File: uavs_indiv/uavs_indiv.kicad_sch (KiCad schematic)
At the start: 16 parts, among them J4 Conn_01x04_Pin, J5 Conn_01x04_Pin, J6 Conn_01x04_Pin, U1 LM2576HVS-5, U3 LM2576HVS-5

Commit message: wtf did i just see
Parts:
- removed J4, J5: Conn_01x04_Pin, customdcdc:Molex_Micro-Fit_3.0_43650-0400_1x04_P3.00mm_Horizontal, symbol Connector:Conn_01x04_Pin
- added J1: Conn_01x02_Socket, Connector_AMASS:AMASS_XT60PW-F_1x02_P7.20mm_Horizontal, symbol Connector:Conn_01x02_Socket
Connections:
- net +5V: now also J6.1 (Pin_1), J6.2 (Pin_2)
- net GND: now also J1.1 (Pin_1)
- net Vin: now also J1.2 (Pin_2); no longer J6.1 (Pin_1), J6.2 (Pin_2)
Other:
- moved on the sheet: C5, C6, J6

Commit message: redidt footprints and routing
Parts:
- added J2, J3: Conn_01x04_Pin, customdcdc:Molex_Micro-Fit_3.0_43650-0400_1x04_P3.00mm_Horizontal, symbol Connector:Conn_01x04_Pin
- C1, C8: value 330uF -> 1000uF; footprint Capacitor_THT:CP_Axial_L29.0mm_D10.0mm_P35.00mm_Horizontal -> customdcdc:capacitor1000uf
- C2, C7: footprint Capacitor_THT:CP_Axial_L29.0mm_D10.0mm_P35.00mm_Horizontal -> customdcdc:capacitor100uf
- C5: footprint Capacitor_THT:CP_Axial_L29.0mm_D10.0mm_P35.00mm_Horizontal -> customdcdc:capacitor220uf
- C6: footprint Capacitor_THT:CP_Axial_L20.0mm_D10.0mm_P26.00mm_Horizontal -> customdcdc:capacitor680uf
- L1, L3: value 330u -> 100u; footprint Inductor_THT:L_Axial_L20.0mm_D8.0mm_P5.08mm_Vertical -> customdcdc:inductor3.5a100u
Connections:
- net +5V: now also J2.1 (Pin_1), J2.2 (Pin_2), J3.1 (Pin_1), J3.2 (Pin_2)
- net GND: now also J2.3 (Pin_3), J2.4 (Pin_4), J3.3 (Pin_3), J3.4 (Pin_4)
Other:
- moved on the sheet: C1, C2, C5, C6, D1, J1, L1, U1

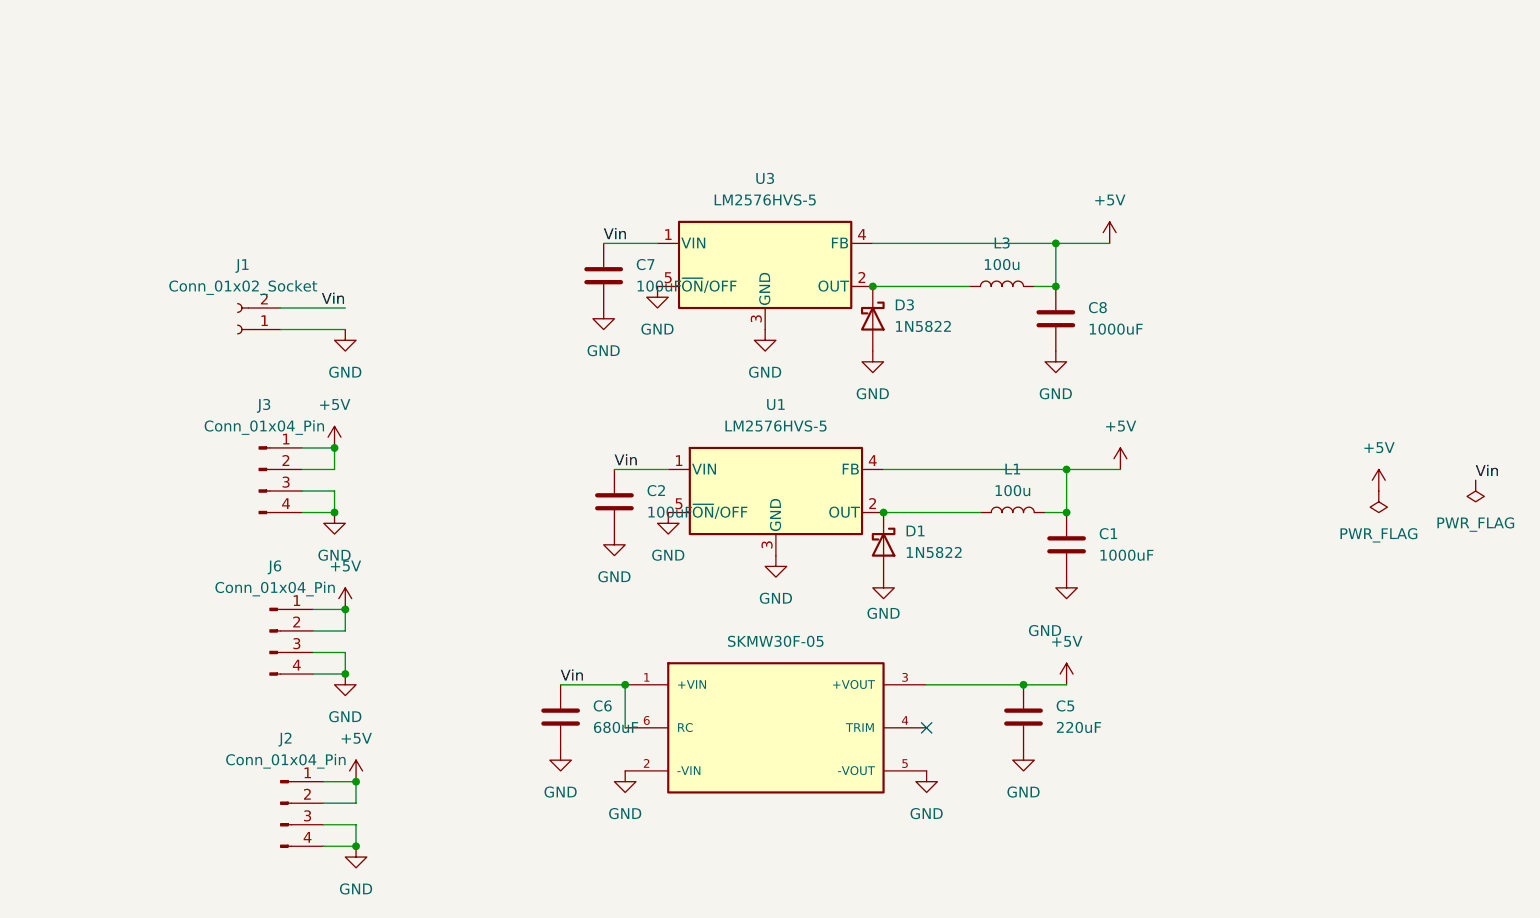
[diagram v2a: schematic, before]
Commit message: made traces bigger added space between components added screw holes added one more 5v output (unisolated)
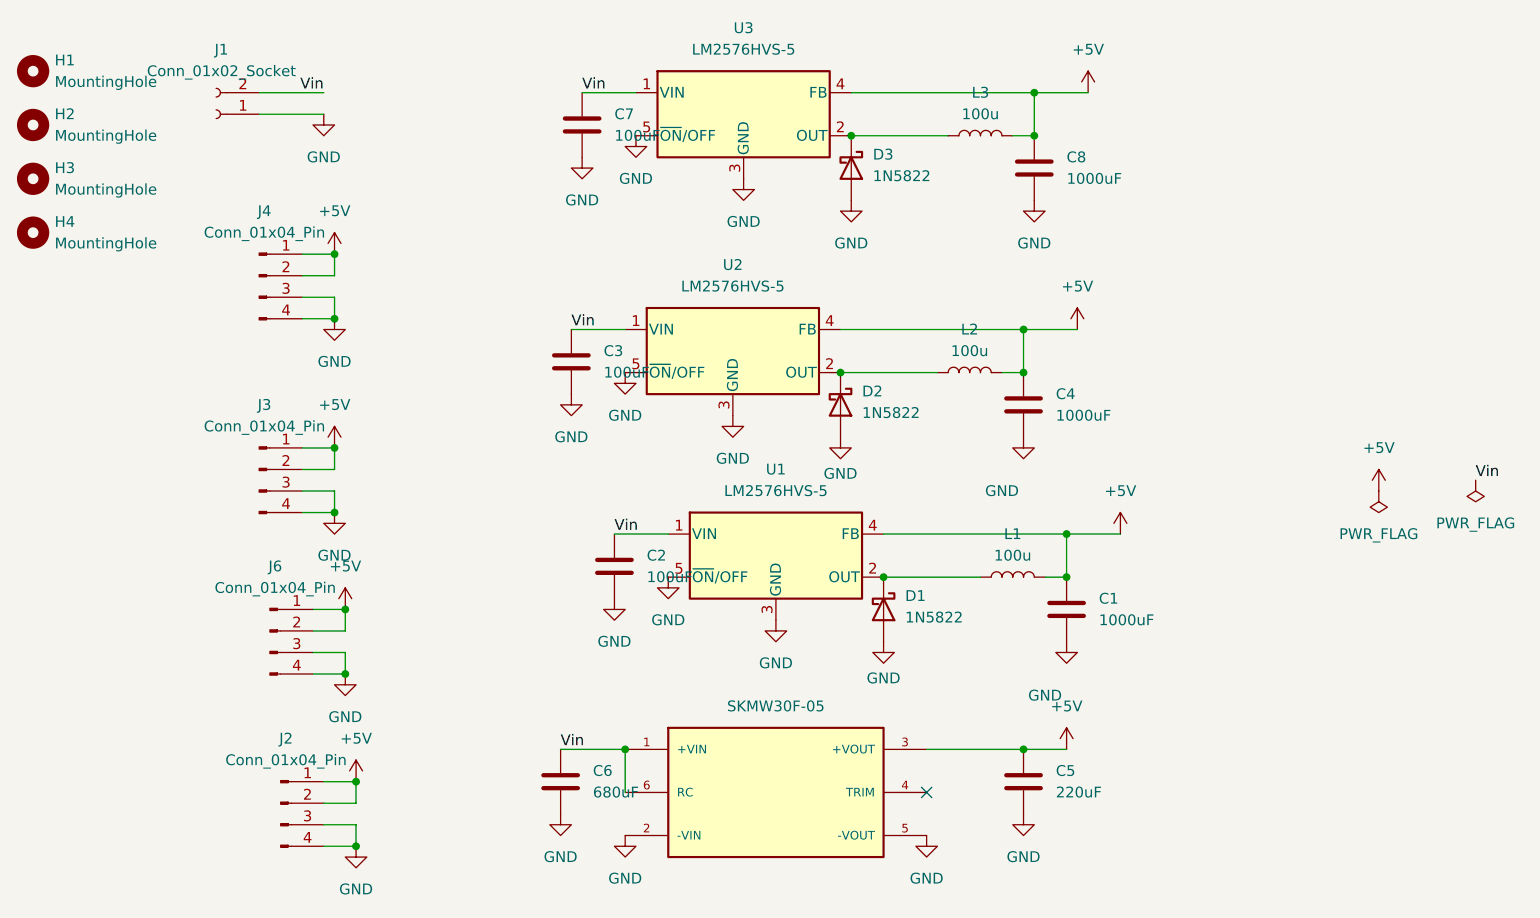
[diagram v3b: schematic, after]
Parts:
- added C3: 100uF, customdcdc:capacitor100uf, symbol Device:C
- added C4: 1000uF, customdcdc:capacitor1000uf, symbol Device:C
- added D2: 1N5822, Diode_THT:D_DO-201AD_P15.24mm_Horizontal, symbol Diode:1N5822
- added H1, H2, H3, H4: MountingHole, MountingHole:MountingHole_2.1mm, symbol Mechanical:MountingHole
- added J4: Conn_01x04_Pin, customdcdc:Molex_Micro-Fit_3.0_43650-0400_1x04_P3.00mm_Horizontal, symbol Connector:Conn_01x04_Pin
- added L2: 100u, customdcdc:inductor3.5a100u, symbol Device:L
- added U2: LM2576HVS-5, Package_TO_SOT_SMD:TO-263-5_TabPin3, symbol Regulator_Switching:LM2576HVS-5
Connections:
- net +5V: now also C4.1, J4.1 (Pin_1), J4.2 (Pin_2), L2.2, U2.4 (FB)
- net GND: now also C3.2, C4.2, D2.2 (A), J4.3 (Pin_3), J4.4 (Pin_4), U2.3 (GND), U2.5 (~{ON}/OFF)
- net Vin: now also C3.1, U2.1 (VIN)
- new net: D2.1 (K), L2.1, U2.2 (OUT)
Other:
- moved on the sheet: C1, C2, C5, C6, C7, C8, D1, D3, J1, L1, L3, U1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
